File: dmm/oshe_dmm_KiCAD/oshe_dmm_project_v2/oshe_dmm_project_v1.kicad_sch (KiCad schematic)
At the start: 101 parts, among them J1 FTDI Basic, J10 Voltage Range 2, J11 Voltage Range 3, J12 Voltage Range 3, J13 DC Current Indication, J14 Continuity, J16 AC Voltage Range 2, J18 AC Voltage Range 3, J2 Voltage, J20 AC Voltage Range 1, J21 AC Current Indication, J22 MJ-3536N, J3 GND, J4 Current, J5 Resistance Meas, J6 ON/OFF, J7 Voltage Range 1, J8 Voltage Range 1, J9 Voltage Range 2, SW1 PTS526 SK15 SMTR2 LFS, U1 ATmega328P-A, U2 AD736, U3 ADS1115IDGS, U4 MAX4617CPE, U5 LM317_SOT-223, U7 TPS60400DBV, U8 ADS1115IDGS, Y1 16MHz

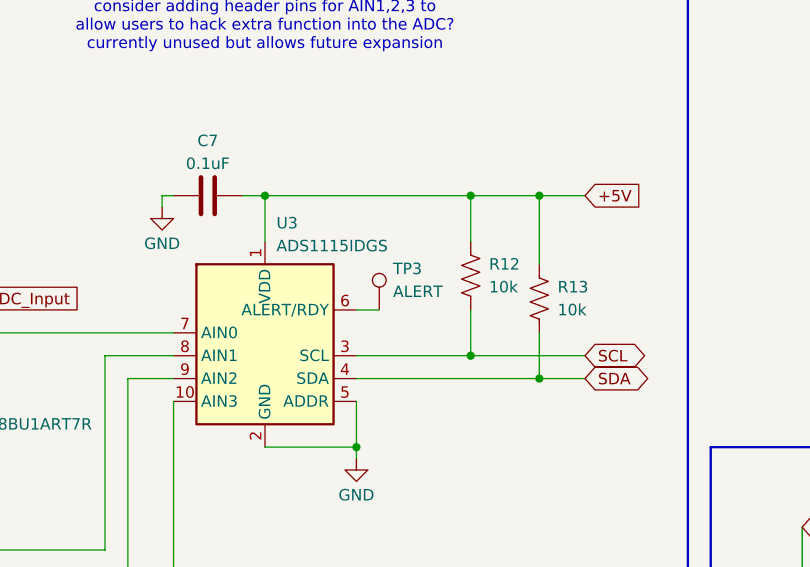
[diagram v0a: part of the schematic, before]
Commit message: Fixed footprint errors
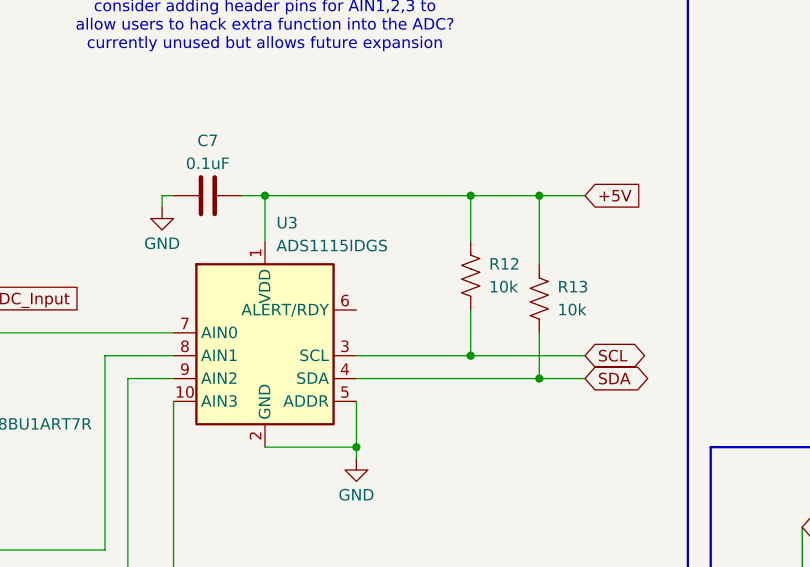
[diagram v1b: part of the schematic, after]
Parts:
- removed TP3: ALERT, TestPoint:TestPoint_Keystone_5019_Minature, symbol Connector:TestPoint
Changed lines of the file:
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@@
 	(wire
 		(pts
-			(xy 144.78 181.61) (xy 147.32 181.61)
-		)
-		(stroke
-			(width 0)
-			(type default)
-		)
-	)
-	(wire
-		(pts
 			(xy 30.48 82.55) (xy 31.75 82.55)
 		)
@@
 					(unit 1)
 				)
-			)
-		)
-	)
-	(symbol
-		(lib_id "Connector:TestPoint")
-		(at 147.32 181.61 0)
-		(unit 1)
-		(exclude_from_sim no)
-		(in_bom yes)
-		(on_board yes)
-		(dnp no)
-		(property "Reference" "TP3"
-			(at 148.844 177.038 0)
-			(effects
-				(font
-					(size 1.27 1.27)
-				)
-				(justify left)
-			)
-		)
-		(property "Value" "ALERT"
-			(at 148.844 179.578 0)
-			(effects
-				(font
-					(size 1.27 1.27)
-				)
-				(justify left)
-			)
-		)
-		(property "Footprint" "TestPoint:TestPoint_Keystone_5019_Minature"
-			(at 152.4 181.61 0)
-			(effects
-				(font
-					(size 1.27 1.27)
-				)
-				(hide yes)
-			)
-		)
-		(property "Datasheet" "~"
-			(at 152.4 181.61 0)
-			(effects
-				(font
-					(size 1.27 1.27)
-				)
-				(hide yes)
-			)
-		)
-		(property "Description" "test point"
-			(at 147.32 181.61 0)
-			(effects
-				(font
-					(size 1.27 1.27)
-				)
-				(hide yes)
-			)
-		)
-		(pin "1"
-		)
-		(instances
-			(project "oshe_dmm_project_v1"
-				(path "/24c8480a-c336-4df0-8536-7016ee8fc0ac"
-					(reference "TP3")
-					(unit 1)
-				)

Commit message: update
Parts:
- R22: value 180 -> 91k
- R23: value 680 -> 39k
- R24: value 1.2k -> 24k
- R25: value R? -> 4.7k
- R34: value R? -> 1.3k
- R36: value 2.4k -> 10k
- R37: value 3k -> 6.8k
- R38: value 1.8k -> 15k
- R39: value R? -> 2.7k
- R8: value 1k -> 10k
- R9: value R? -> 220
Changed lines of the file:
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@@
 			)
 		)
-		(property "Value" "680"
+		(property "Value" "39k"
 			(at 323.85 138.4299 0)
 			(effects
@@
 			)
 		)
-		(property "Value" "1.8k"
+		(property "Value" "15k"
 			(at 372.11 110.4899 0)
 			(effects
@@
 			)
 		)
-		(property "Value" "R?"
+		(property "Value" "4.7k"
 			(at 323.85 187.9599 0)
 			(effects
@@
 			)
 		)
-		(property "Value" "1.2k"
+		(property "Value" "24k"
 			(at 323.85 166.3699 0)
 			(effects
@@
 			)
 		)
-		(property "Value" "R?"
+		(property "Value" "220"
 			(at 373.38 210.8199 0)
 			(effects
@@
 			)
 		)
-		(property "Value" "3k"
+		(property "Value" "6.8k"
 			(at 372.11 167.6399 0)
 			(effects
@@
 			)
 		)
-		(property "Value" "2.4k"
+		(property "Value" "10k"
 			(at 372.11 138.4299 0)
 			(effects
@@
 			)
 		)
-		(property "Value" "1k"
+		(property "Value" "10k"
 			(at 351.79 229.8699 0)
 			(effects
@@
 			)
 		)
-		(property "Value" "R?"
+		(property "Value" "1.3k"
 			(at 372.11 186.6899 0)
 			(effects
@@
 			)
 		)
-		(property "Value" "R?"
+		(property "Value" "2.7k"
 			(at 325.12 209.5499 0)
 			(effects
@@
 			)
 		)
-		(property "Value" "180"
+		(property "Value" "91k"
 			(at 323.85 110.4899 0)
 			(effects
